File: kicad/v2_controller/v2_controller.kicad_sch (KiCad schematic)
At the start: 5 parts, among them J1 Conn_Left, J2 Conn_Right, J3 Conn_Numpad, J4 Conn_01x04, U1 ESP32-S3-DevKitC

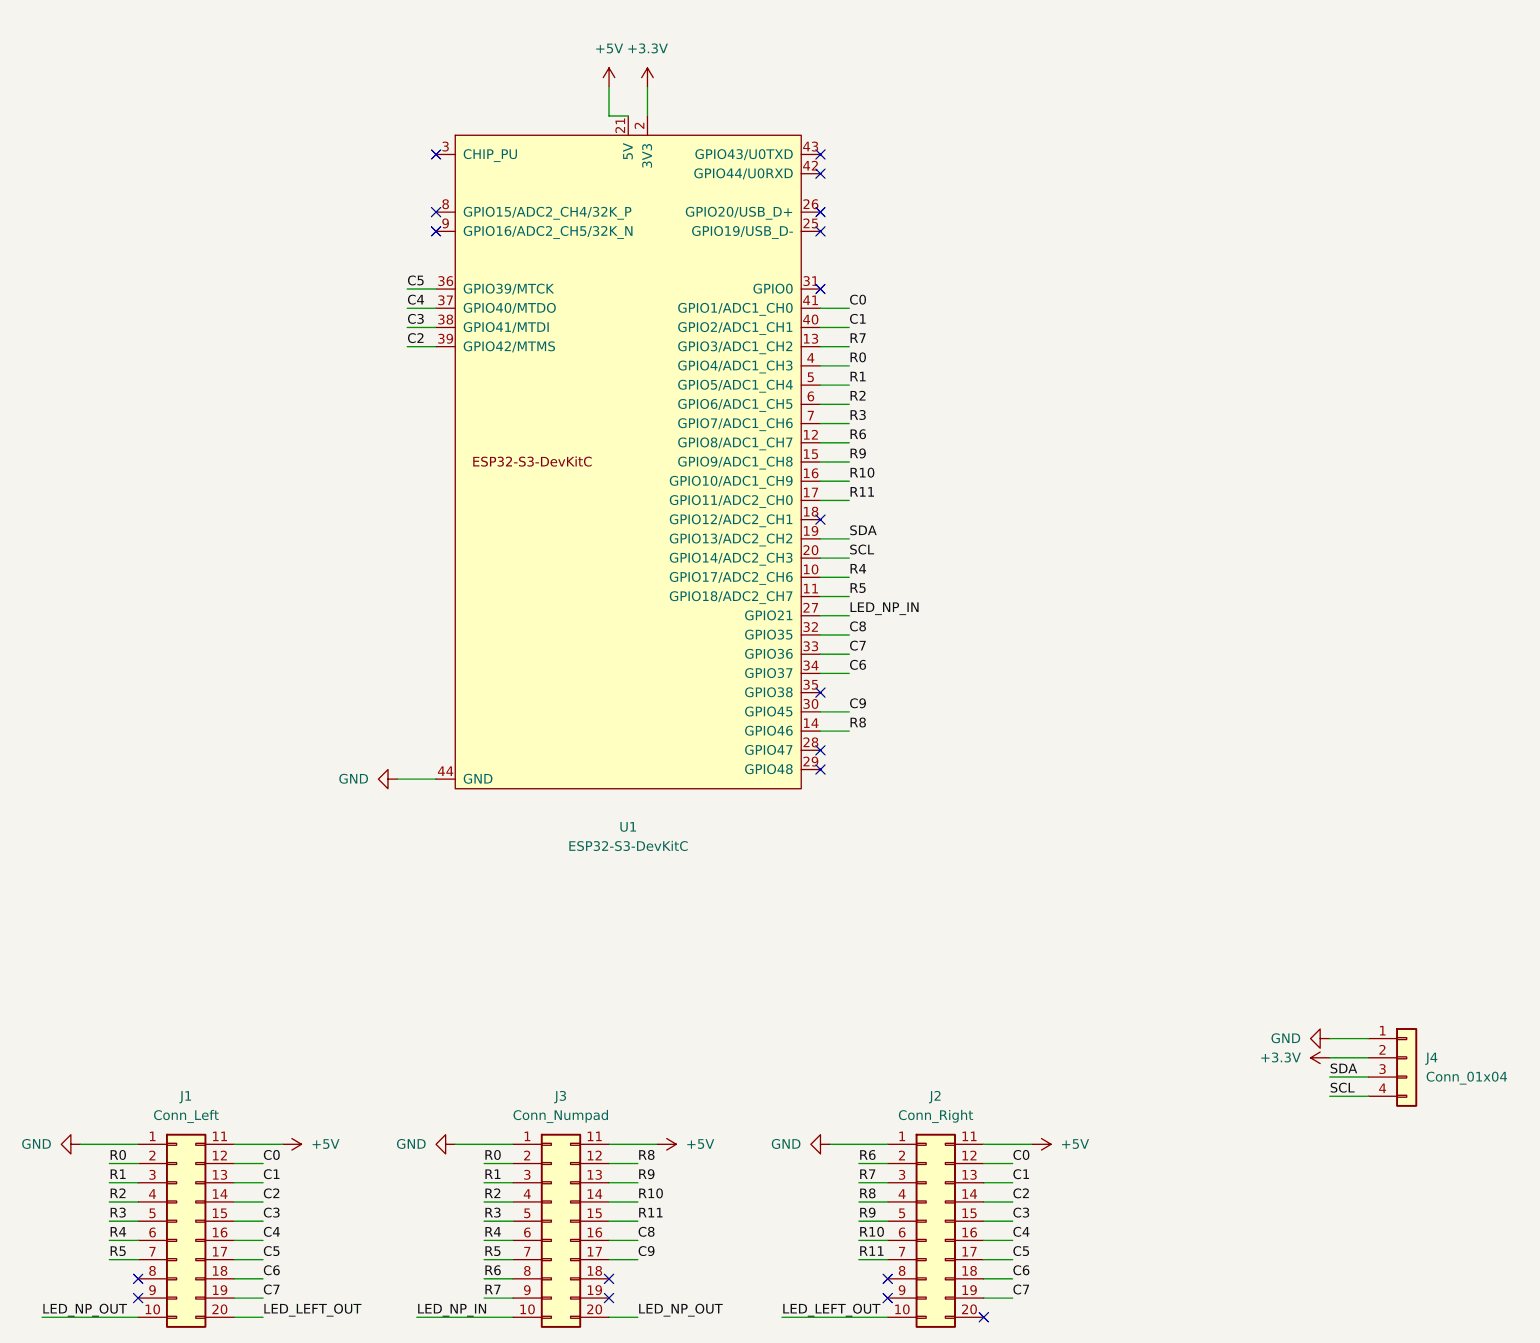
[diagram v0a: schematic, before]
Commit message: [kicad] update schematic for v2 controller
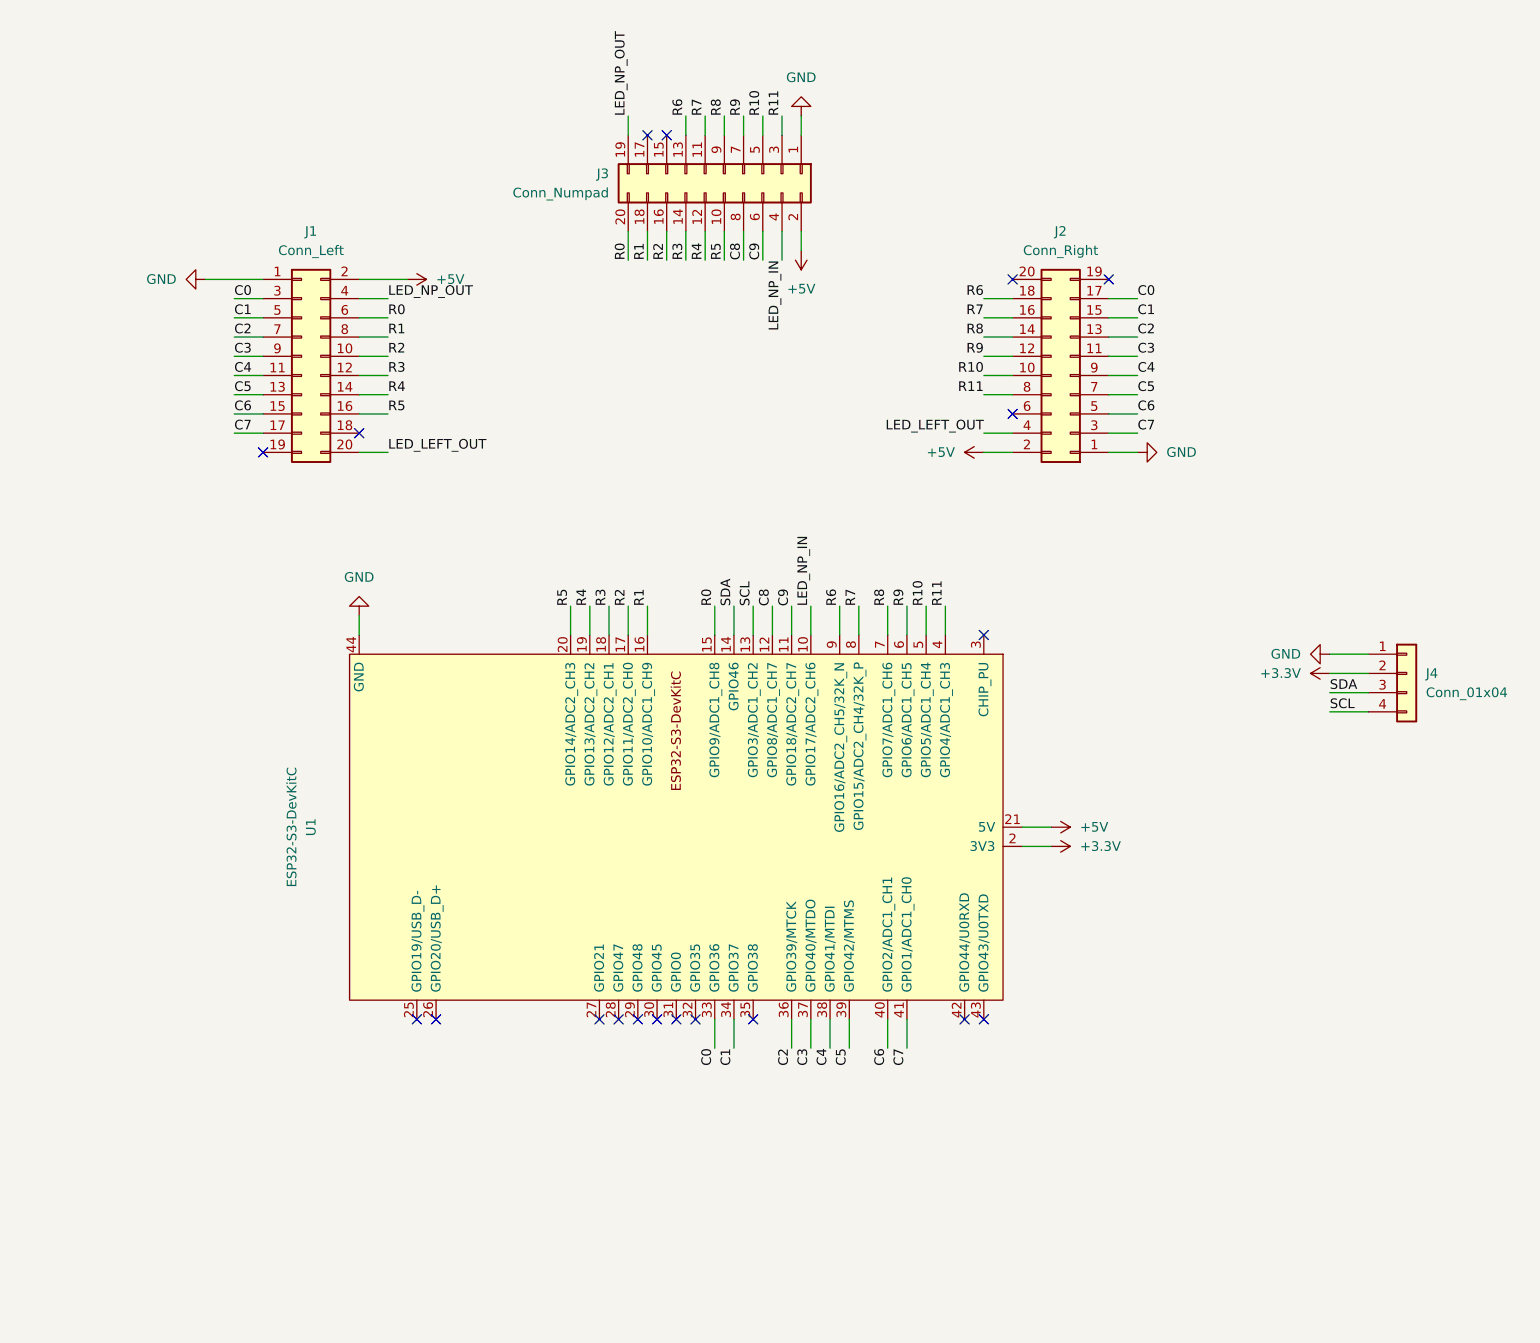
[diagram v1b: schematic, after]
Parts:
- removed J1: Conn_Left, Connector_IDC:IDC-Header_2x10_P2.54mm_Vertical, symbol Connector_Generic:Conn_02x10_Top_Bottom
- removed J2: Conn_Right, Connector_IDC:IDC-Header_2x10_P2.54mm_Vertical, symbol Connector_Generic:Conn_02x10_Top_Bottom
- removed J3: Conn_Numpad, Connector_IDC:IDC-Header_2x10_P2.54mm_Vertical, symbol Connector_Generic:Conn_02x10_Top_Bottom
- added J1: Conn_Left, Connector_IDC:IDC-Header_2x10_P2.54mm_Vertical, symbol Connector_Generic:Conn_02x10_Odd_Even
- added J2: Conn_Right, Connector_IDC:IDC-Header_2x10_P2.54mm_Vertical, symbol Connector_Generic:Conn_02x10_Odd_Even
- added J3: Conn_Numpad, Connector_IDC:IDC-Header_2x10_P2.54mm_Vertical, symbol Connector_Generic:Conn_02x10_Odd_Even
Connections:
- net +5V: now also J1.2 (Pin_2), J2.2 (Pin_2), J3.2 (Pin_2)
- net C0: now also U1.33 (GPIO36), J1.3 (Pin_3), J2.17 (Pin_17); no longer U1.41 (GPIO1/ADC1_CH0)
- net C1: now also U1.34 (GPIO37), J1.5 (Pin_5), J2.15 (Pin_15); no longer U1.40 (GPIO2/ADC1_CH1)
- net C2: now also U1.36 (GPIO39/MTCK), J1.7 (Pin_7), J2.13 (Pin_13); no longer U1.39 (GPIO42/MTMS)
- net C3: now also U1.37 (GPIO40/MTDO), J1.9 (Pin_9), J2.11 (Pin_11); no longer U1.38 (GPIO41/MTDI)
- net C4: now also U1.38 (GPIO41/MTDI), J1.11 (Pin_11), J2.9 (Pin_9); no longer U1.37 (GPIO40/MTDO)
- net C5: now also U1.39 (GPIO42/MTMS), J1.13 (Pin_13), J2.7 (Pin_7); no longer U1.36 (GPIO39/MTCK)
- net C6: now also U1.40 (GPIO2/ADC1_CH1), J1.15 (Pin_15), J2.5 (Pin_5); no longer U1.34 (GPIO37)
- net C7: now also U1.41 (GPIO1/ADC1_CH0), J1.17 (Pin_17), J2.3 (Pin_3); no longer U1.33 (GPIO36)
- net C8: now also U1.12 (GPIO8/ADC1_CH7), J3.8 (Pin_8); no longer U1.32 (GPIO35)
- net C9: now also U1.11 (GPIO18/ADC2_CH7), J3.6 (Pin_6); no longer U1.30 (GPIO45)
- net GND: now also J1.1 (Pin_1), J2.1 (Pin_1), J3.1 (Pin_1)
- net LED_LEFT_OUT: now also J1.20 (Pin_20), J2.4 (Pin_4)
- net LED_NP_IN: now also U1.10 (GPIO17/ADC2_CH6), J3.4 (Pin_4); no longer U1.27 (GPIO21)
- net LED_NP_OUT: now also J1.4 (Pin_4), J3.19 (Pin_19)
- net R0: now also U1.15 (GPIO9/ADC1_CH8), J1.6 (Pin_6), J3.20 (Pin_20); no longer U1.4 (GPIO4/ADC1_CH3)
- net R1: now also U1.16 (GPIO10/ADC1_CH9), J1.8 (Pin_8), J3.18 (Pin_18); no longer U1.5 (GPIO5/ADC1_CH4)
- net R10: now also U1.5 (GPIO5/ADC1_CH4), J2.10 (Pin_10), J3.5 (Pin_5); no longer U1.16 (GPIO10/ADC1_CH9)
- net R11: now also U1.4 (GPIO4/ADC1_CH3), J2.8 (Pin_8), J3.3 (Pin_3); no longer U1.17 (GPIO11/ADC2_CH0)
- net R2: now also U1.17 (GPIO11/ADC2_CH0), J1.10 (Pin_10), J3.16 (Pin_16); no longer U1.6 (GPIO6/ADC1_CH5)
- net R3: now also U1.18 (GPIO12/ADC2_CH1), J1.12 (Pin_12), J3.14 (Pin_14); no longer U1.7 (GPIO7/ADC1_CH6)
- net R4: now also U1.19 (GPIO13/ADC2_CH2), J1.14 (Pin_14), J3.12 (Pin_12); no longer U1.10 (GPIO17/ADC2_CH6)
- net R5: now also U1.20 (GPIO14/ADC2_CH3), J1.16 (Pin_16), J3.10 (Pin_10); no longer U1.11 (GPIO18/ADC2_CH7)
- net R6: now also U1.9 (GPIO16/ADC2_CH5/32K_N), J2.18 (Pin_18), J3.13 (Pin_13); no longer U1.12 (GPIO8/ADC1_CH7)
- net R7: now also U1.8 (GPIO15/ADC2_CH4/32K_P), J2.16 (Pin_16), J3.11 (Pin_11); no longer U1.13 (GPIO3/ADC1_CH2)
- net R8: now also U1.7 (GPIO7/ADC1_CH6), J2.14 (Pin_14), J3.9 (Pin_9); no longer U1.14 (GPIO46)
- net R9: now also U1.6 (GPIO6/ADC1_CH5), J2.12 (Pin_12), J3.7 (Pin_7); no longer U1.15 (GPIO9/ADC1_CH8)
- net SCL: now also U1.13 (GPIO3/ADC1_CH2); no longer U1.20 (GPIO14/ADC2_CH3)
- net SDA: now also U1.14 (GPIO46); no longer U1.19 (GPIO13/ADC2_CH2)
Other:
- moved on the sheet: J4, U1
